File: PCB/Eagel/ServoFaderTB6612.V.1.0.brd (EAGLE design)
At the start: 147.1 x 17.8 mm, 29 parts, among them IC1 ATTINY804-SSNR, IC2 AT42QT1010, IC4 SN74LVC1G14DBVR, IC5 TB6612FNG,C,8,EL

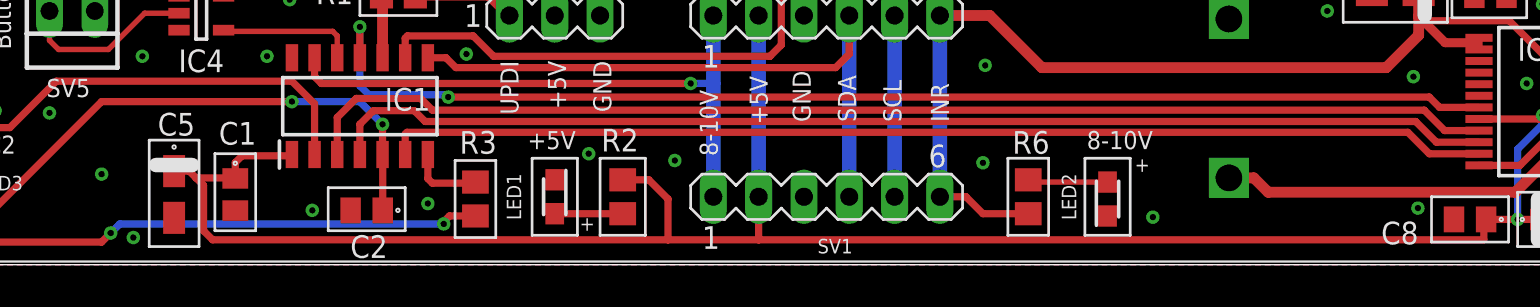
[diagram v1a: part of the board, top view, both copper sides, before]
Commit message: Update Pin PB3
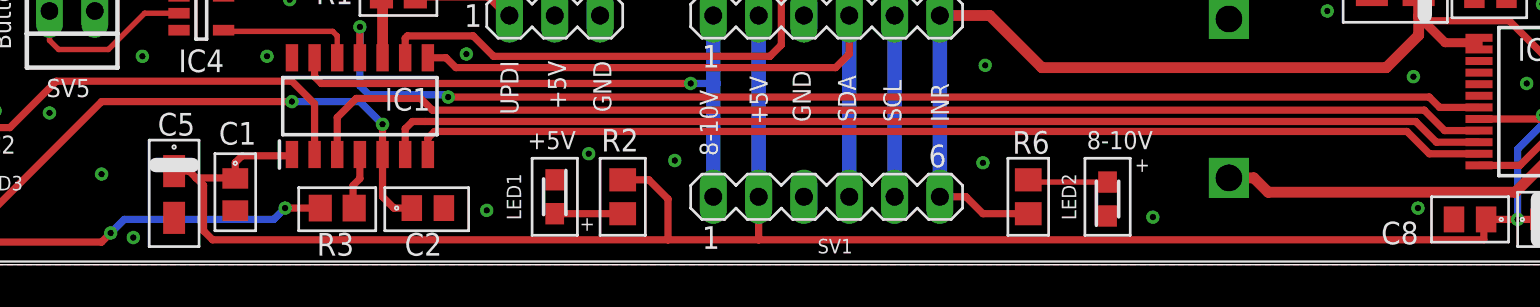
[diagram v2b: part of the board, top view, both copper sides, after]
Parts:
- moved R3 7.76 mm to (53.8, 3.17), turned to 0 degrees
- moved C2 3.43 mm to (58.9, 3.17), turned to 0 degrees
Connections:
- removed net N$6: IC1.7, R3.2
- new net N$5: IC1.4, R3.2
- net AIN2: now also IC1.6; no longer IC1.4
- net PWM: now also IC1.7; no longer IC1.6
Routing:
- net D-OUT: track 67.3 -> 58.7 mm
- net N$6: track 4.15 -> 0.00 mm
- net AIN2: track 65.5 -> 62.3 mm
- net N$5: track 0.00 -> 3.19 mm
- net PWM: track 61.9 -> 60.5 mm
- net SERVOTRACK: track 56.3 -> 57.1 mm
- net GND: vias 30 -> 29

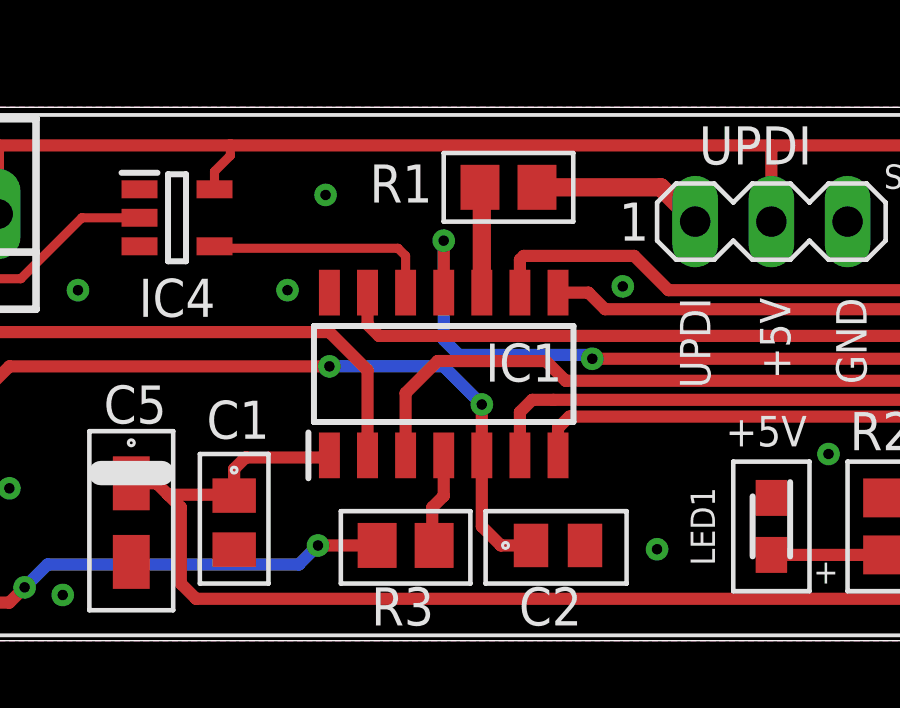
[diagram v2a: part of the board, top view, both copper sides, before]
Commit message: Update
Motorsteuerung mit ABS eingefügt
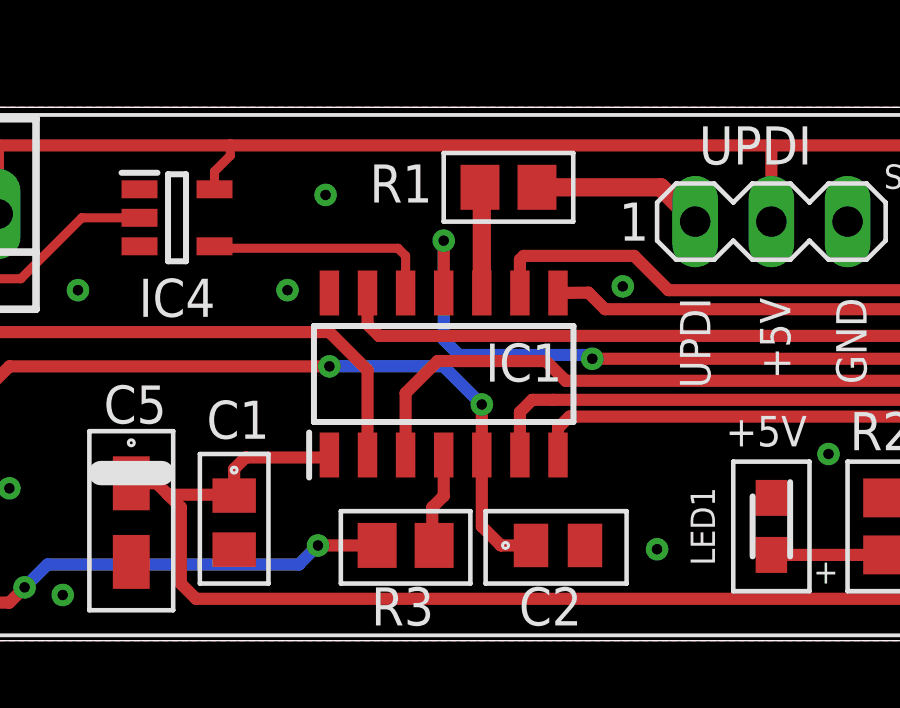
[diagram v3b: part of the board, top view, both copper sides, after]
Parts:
- IC1: value ATTINY804-SSNR -> ATTINY1604-SSN
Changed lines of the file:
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@@
 <drawing>
 <settings>
-<setting alwaysvectorfont="yes"/>
+<setting alwaysvectorfont="no"/>
 <setting verticaltext="up"/>
 </settings>
@@
 <attribute name="NAME" x="31.369" y="14.605" size="1.27" layer="25" rot="R180" align="center"/>
 </element>
-<element name="IC1" library="SamacSys_Parts" package="SOIC127P600X175-14N" value="ATTINY804-SSNR" x="55.118" y="8.89" smashed="yes" rot="R90">
-<attribute name="DESCRIPTION" value="8-bit Microcontrollers - MCU 20MHz, 8KB, SOIC14, Ind 105C, Green, T&amp;R" x="79.248" y="41.91" size="1.778" layer="27" rot="R90" display="off"/>
+<element name="IC1" library="SamacSys_Parts" package="SOIC127P600X175-14N" value="ATTINY1604-SSN" x="55.118" y="8.89" smashed="yes" rot="R90">
+<attribute name="DESCRIPTION" value="8-bit Microcontrollers - MCU 20MHz, 16KB, SOIC14, Ind 105C, Green, Tube" x="79.248" y="41.91" size="1.778" layer="27" rot="R90" display="off"/>
 <attribute name="HEIGHT" value="1.75mm" x="79.248" y="41.91" size="1.778" layer="27" rot="R90" display="off"/>
 <attribute name="MANUFACTURER_NAME" value="Microchip" x="79.248" y="41.91" size="1.778" layer="27" rot="R90" display="off"/>
-<attribute name="MANUFACTURER_PART_NUMBER" value="ATTINY804-SSNR" x="79.248" y="41.91" size="1.778" layer="27" rot="R90" display="off"/>
-<attribute name="MOUSER_PART_NUMBER" value="556-ATTINY804-SSNR" x="79.248" y="41.91" size="1.778" layer="27" rot="R90" display="off"/>
-<attribute name="MOUSER_PRICE-STOCK" value="https://www.mouser.co.uk/ProductDetail/Microchip-Technology/ATTINY804-SSNR?qs=T3oQrply3y%252BBKoVZpNVlTw%3D%3D" x="79.248" y="41.91" size="1.778" layer="27" rot="R90" display="off"/>
+<attribute name="MANUFACTURER_PART_NUMBER" value="ATTINY1604-SSN" x="79.248" y="41.91" size="1.778" layer="27" rot="R90" display="off"/>
+<attribute name="MOUSER_PART_NUMBER" value="556-ATTINY1604-SSN" x="79.248" y="41.91" size="1.778" layer="27" rot="R90" display="off"/>
+<attribute name="MOUSER_PRICE-STOCK" value="https://www.mouser.co.uk/ProductDetail/Microchip-Technology-Atmel/ATTINY1604-SSN?qs=T3oQrply3y8tu5s3g%2F7NqA%3D%3D" x="79.248" y="41.91" size="1.778" layer="27" rot="R90" display="off"/>
 <attribute name="NAME" x="57.785" y="9.271" size="1.27" layer="25" rot="R180" align="center"/>
 </element>
@@
 <contactref element="SV1" pad="5"/>
 <contactref element="SV2" pad="5"/>
-<wire x1="57.658" y1="11.602" x2="57.658" y2="12.7" width="0.4064" layer="1"/>
+<wire x1="57.658" y1="11.59" x2="57.658" y2="12.7" width="0.4064" layer="1"/>
 <wire x1="57.658" y1="12.7" x2="57.785" y2="12.827" width="0.4064" layer="1"/>
 <wire x1="61.468" y1="12.827" x2="62.611" y2="11.684" width="0.4064" layer="1"/>
@@
 <wire x1="81.788" y1="11.049" x2="60.497" y2="11.049" width="0.4064" layer="1"/>
 <wire x1="60.497" y1="11.049" x2="59.944" y2="11.602" width="0.4064" layer="1"/>
-<wire x1="59.944" y1="11.602" x2="58.928" y2="11.602" width="0.4064" layer="1"/>
+<wire x1="59.944" y1="11.602" x2="58.928" y2="11.59" width="0.4064" layer="1"/>
 <wire x1="82.55" y1="11.811" x2="81.788" y2="11.049" width="0.4064" layer="1"/>
 <wire x1="82.55" y1="13.97" x2="82.55" y2="3.81" width="0.8128" layer="16"/>
@@
 <wire x1="115.925" y1="7.519" x2="117.85" y2="7.519" width="0.4064" layer="1"/>
 <wire x1="114.7798" y1="8.6642" x2="115.925" y2="7.519" width="0.4064" layer="1"/>
-<wire x1="53.848" y1="6.178" x2="53.848" y2="8.255" width="0.4064" layer="1"/>
+<wire x1="53.848" y1="6.19" x2="53.848" y2="8.255" width="0.4064" layer="1"/>
 <wire x1="58.52446875" y1="9.3218" x2="59.18206875" y2="8.6642" width="0.4064" layer="1"/>
 <wire x1="54.9148" y1="9.3218" x2="58.52446875" y2="9.3218" width="0.4064" layer="1"/>
@@
 <wire x1="115.066" y1="6.219" x2="117.85" y2="6.219" width="0.4064" layer="1"/>
 <contactref element="IC1" pad="7"/>
-<wire x1="58.928" y1="6.178" x2="58.928" y2="7.0894" width="0.4064" layer="1"/>
+<wire x1="58.928" y1="6.19" x2="58.928" y2="7.0894" width="0.4064" layer="1"/>
 <wire x1="58.928" y1="7.0894" x2="59.309" y2="7.4704" width="0.4064" layer="1"/>
 <wire x1="59.309" y1="7.4704" x2="113.8146" y2="7.4704" width="0.4064" layer="1"/>
@@
 <contactref element="IC1" pad="6"/>
 <wire x1="58.7728" y1="8.0292" x2="58.0672" y2="8.0292" width="0.4064" layer="1"/>
-<wire x1="57.658" y1="7.62" x2="57.658" y2="6.178" width="0.4064" layer="1"/>
+<wire x1="57.658" y1="7.62" x2="57.658" y2="6.19" width="0.4064" layer="1"/>
 <wire x1="58.0672" y1="8.0292" x2="57.658" y2="7.62" width="0.4064" layer="1"/>
 </signal>
@@
 <wire x1="58.028" y1="3.175" x2="57.023" y2="3.175" width="0.4064" layer="1"/>
 <wire x1="57.023" y1="3.175" x2="56.388" y2="3.81" width="0.4064" layer="1"/>
-<wire x1="56.388" y1="6.178" x2="56.388" y2="3.81" width="0.4064" layer="1"/>
+<wire x1="56.388" y1="6.19" x2="56.388" y2="3.81" width="0.4064" layer="1"/>
 <wire x1="34.2265" y1="2.7305" x2="40.64" y2="9.144" width="0.4064" layer="1"/>
 <wire x1="51.308" y1="9.144" x2="40.64" y2="9.144" width="0.4064" layer="1"/>
@@
 <wire x1="55.118" y1="9.144" x2="56.388" y2="7.874" width="0.4064" layer="16"/>
 <via x="56.388" y="7.874" extent="1-16" drill="0.35"/>
-<wire x1="56.388" y1="7.874" x2="56.388" y2="6.178" width="0.4064" layer="1"/>
+<wire x1="56.388" y1="7.874" x2="56.388" y2="6.19" width="0.4064" layer="1"/>
 <wire x1="34.2265" y1="2.7305" x2="21.9075" y2="2.7305" width="0.4064" layer="1"/>
 <wire x1="13.134" y1="3.228" x2="10.591" y2="3.228" width="0.4064" layer="1"/>
@@
 <wire x1="48.514" y1="6.107" x2="48.133" y2="5.726" width="0.4064" layer="1"/>
 <wire x1="48.133" y1="4.837" x2="48.133" y2="5.726" width="0.4064" layer="1"/>
-<wire x1="51.237" y1="6.107" x2="51.308" y2="6.178" width="0.4064" layer="1"/>
+<wire x1="51.237" y1="6.107" x2="51.308" y2="6.19" width="0.4064" layer="1"/>
 <contactref element="SV3" pad="2"/>
 <wire x1="72.39" y1="3.683" x2="72.39" y2="1.397" width="0.4064" layer="1"/>
@@
 <contactref element="R1" pad="1"/>
 <wire x1="56.327" y1="15.113" x2="56.388" y2="15.052" width="0.6096" layer="1"/>
-<wire x1="56.388" y1="15.052" x2="56.388" y2="11.602" width="0.6096" layer="1"/>
+<wire x1="56.388" y1="15.052" x2="56.388" y2="11.59" width="0.6096" layer="1"/>
 </signal>
 <signal name="UPDI">
@@
 <signal name="INR">
 <contactref element="IC1" pad="13"/>
-<wire x1="52.578" y1="11.602" x2="52.578" y2="10.541" width="0.4064" layer="1"/>
+<wire x1="52.578" y1="11.59" x2="52.578" y2="10.541" width="0.4064" layer="1"/>
 <wire x1="52.578" y1="10.541" x2="52.959" y2="10.16" width="0.4064" layer="1"/>
 <contactref element="SV1" pad="1"/>
@@
 <wire x1="25.085" y1="4.572" x2="25.085" y2="5.4" width="0.3048" layer="1"/>
 <wire x1="25.085" y1="5.4" x2="25.654" y2="5.969" width="0.3048" layer="1"/>
-<wire x1="52.578" y1="6.178" x2="52.578" y2="9.017" width="0.4064" layer="1"/>
+<wire x1="52.578" y1="6.19" x2="52.578" y2="9.017" width="0.4064" layer="1"/>
 <wire x1="52.578" y1="9.017" x2="51.308" y2="10.287" width="0.4064" layer="1"/>
 <wire x1="51.308" y1="10.287" x2="38.1" y2="10.287" width="0.4064" layer="1"/>
@@
 <contactref element="IC1" pad="11"/>
 <contactref element="IC5" pad="19"/>
-<wire x1="55.118" y1="11.602" x2="55.118" y2="13.335" width="0.4064" layer="1"/>
+<wire x1="55.118" y1="11.59" x2="55.118" y2="13.335" width="0.4064" layer="1"/>
 <via x="55.118" y="13.335" extent="1-16" drill="0.35"/>
 <wire x1="55.118" y1="13.335" x2="55.118" y2="10.033" width="0.4064" layer="16"/>
@@
 <signal name="N$4">
 <contactref element="IC1" pad="12"/>
-<wire x1="53.848" y1="11.602" x2="53.848" y2="12.827" width="0.3048" layer="1"/>
+<wire x1="53.848" y1="11.59" x2="53.848" y2="12.827" width="0.3048" layer="1"/>
 <wire x1="53.594" y1="13.081" x2="53.848" y2="12.827" width="0.3048" layer="1"/>
 <wire x1="53.594" y1="13.081" x2="47.544" y2="13.081" width="0.3048" layer="1"/>
@@
 <contactref element="IC1" pad="4"/>
 <contactref element="R3" pad="2"/>
-<wire x1="55.118" y1="6.178" x2="55.118" y2="4.826" width="0.4064" layer="1"/>
+<wire x1="55.118" y1="6.19" x2="55.118" y2="4.826" width="0.4064" layer="1"/>
 <wire x1="55.118" y1="4.826" x2="54.737" y2="4.445" width="0.4064" layer="1"/>
 <wire x1="54.737" y1="4.445" x2="54.737" y2="3.236" width="0.4064" layer="1"/>
